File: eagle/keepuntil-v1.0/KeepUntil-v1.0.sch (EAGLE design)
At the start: 12 parts, among them Q1 CSTCR6M00G53Z, U1 ATMEGA328P-AU

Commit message: schematic work
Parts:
- added C4, C5, C6, C7: (no value), resistor:C-EUC0805
- added IC1: REG1117, burr-brown:REG1117
- added ISP, KEYPAD: (no value), pinhead:PINHD-2X3
- added LED1: (no value), led:LEDSMT1206
- added LOCK-CTRL: (no value), pinhead:PINHD-2X4
- added R7: (no value), resistor:R-EU_R0805
- added SERIAL: (no value), pinhead:PINHD-1X3
- added T1: BC846, transistor:BC846
- added X1: MINI-USB-32005-201, con-cypressindustries:MINI-USB-32005-201
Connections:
- removed net N$3: R1.1, S1.1, U1.PC6
- new net 3.3V: C2.2, C4.2, C5.2, C7.2, IC1.GND, ISP.6, LED1.C, S1.2, SERIAL.3, X1.5
- new net COL1: KEYPAD.2, U1.PB0
- new net COL2: KEYPAD.4, U1.PB1
- new net COL3: KEYPAD.6, U1.PB2
- new net LEDGRN: LOCK-CTRL.7, U1.PC0
- new net LEDRED: LOCK-CTRL.8, U1.PC1
- new net MISO: ISP.5, U1.PB4
- new net MOSI: ISP.1, U1.PB3
- new net N$12: LOCK-CTRL.2
- new net N$13: LOCK-CTRL.4
- new net N$5: C4.1, IC1.VIN, X1.1
- new net N$6: C1.2, C3.1
- new net N$7: LED1.A, R7.1
- new net N$8: C5.1, U1.AREF
- new net N$9: LOCK-CTRL.5
- new net RESET: ISP.4, R1.1, S1.1, U1.PC6
- new net ROW1: KEYPAD.1, U1.PD5
- new net ROW2: KEYPAD.3, U1.PD6
- new net ROW3: KEYPAD.5, U1.PD7
- new net RX: SERIAL.1, U1.PD0
- new net SCK: ISP.3, U1.PB5
- new net SCL: U1.PC5
- new net SERVO: LOCK-CTRL.1, U1.PD3
- new net SOLENOID: U1.PD2
- new net TX: SERIAL.2, U1.PD1
- new net VCC: C2.1, C7.1, IC1.VOUT, ISP.2, LOCK-CTRL.3, R1.2, R7.2, U1.AVCC, U1.VCC, U1.VCC_2
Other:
- moved on the sheet: C1, C2, C3, Q1, R1, R2, R3, R4, R5, R6

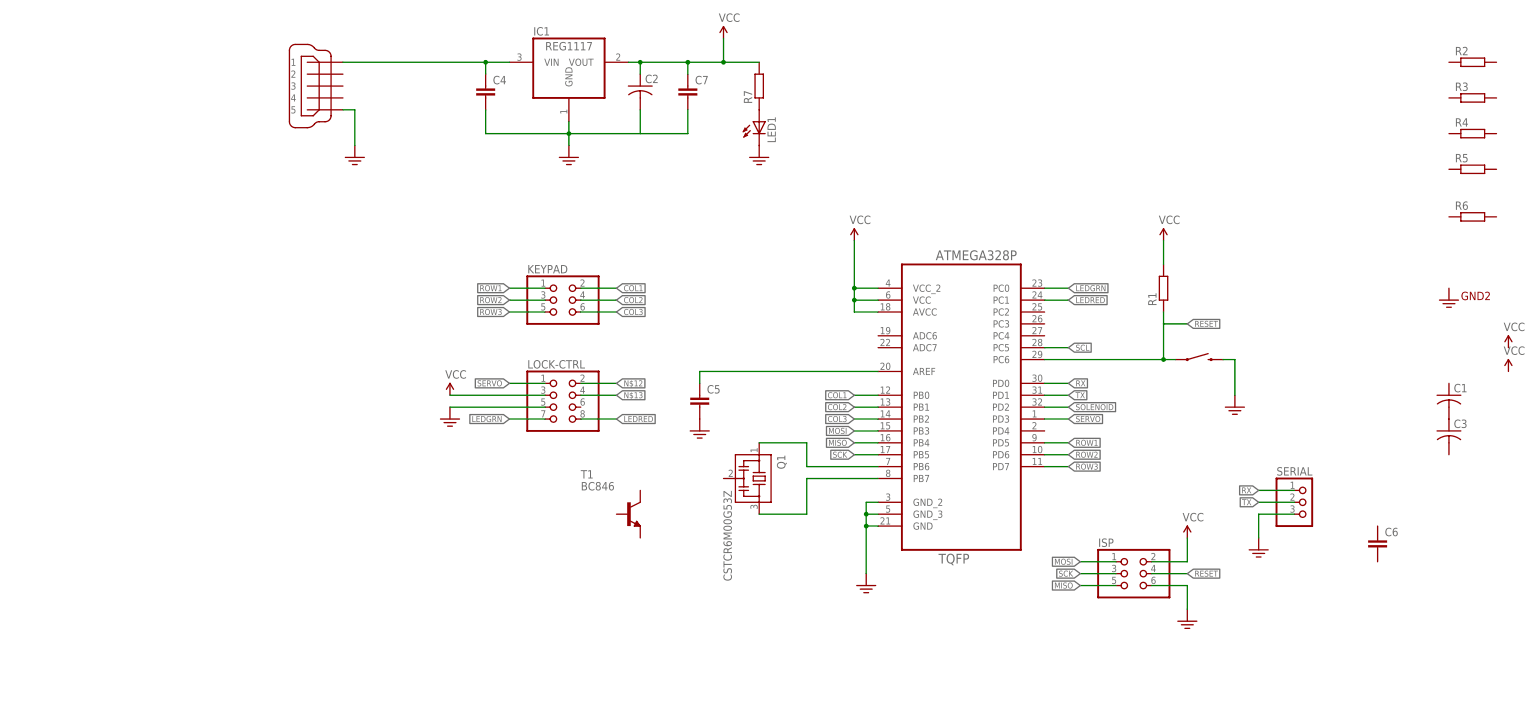
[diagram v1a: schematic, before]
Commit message: remove unnecessary eagle file
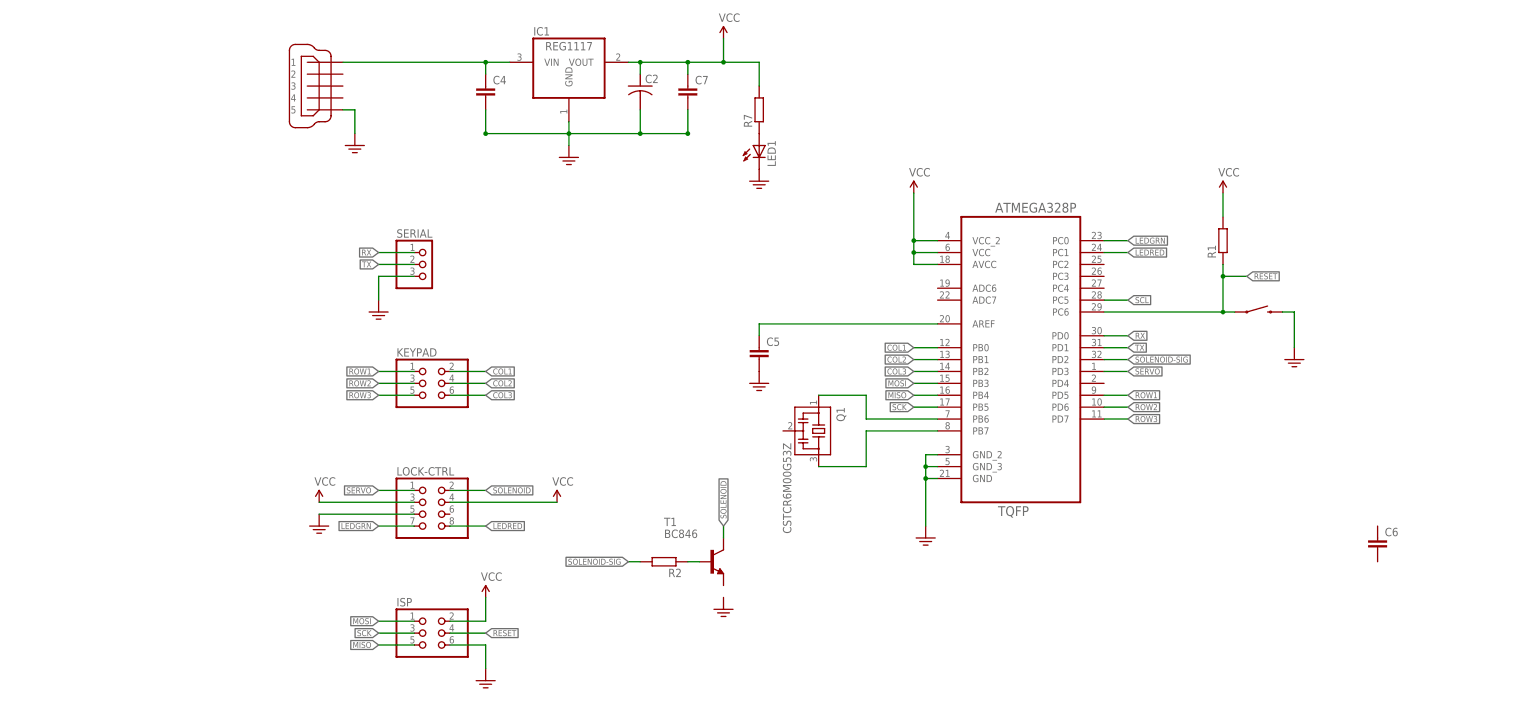
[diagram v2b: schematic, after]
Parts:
- removed C1, C3: (no value), resistor:C-USC1206
- removed R3, R4, R5, R6: (no value), resistor:R-EU_R0805
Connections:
- removed net N$12: LOCK-CTRL.2
- removed net N$13: LOCK-CTRL.4
- removed net N$6: C1.2, C3.1
- new net N$3: R2.1, T1.B
- new net SOLENOID-SIG: R2.2, U1.PD2
- net SOLENOID: now also LOCK-CTRL.2, T1.C; no longer U1.PD2
- net VCC: now also LOCK-CTRL.4
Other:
- moved on the sheet: C5, ISP, KEYPAD, LED1, LOCK-CTRL, Q1, R1, R2, R7, SERIAL, T1

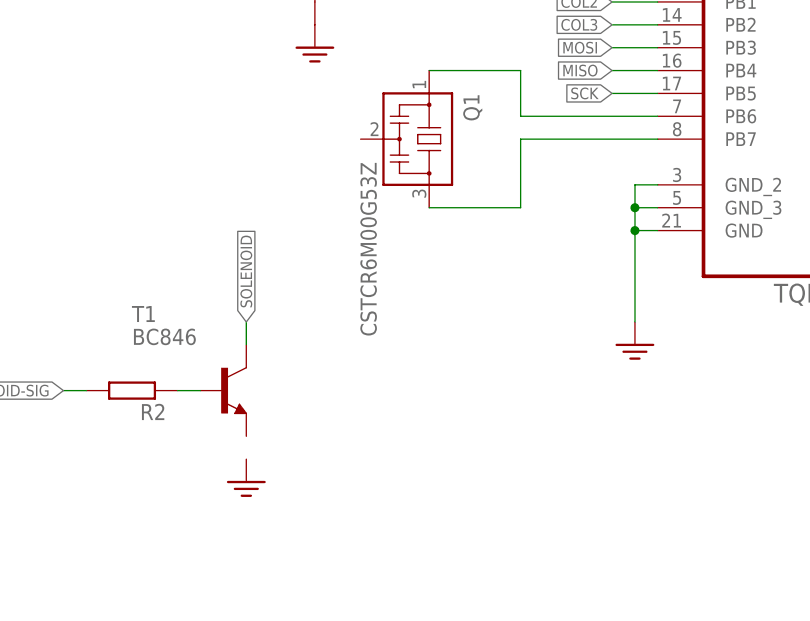
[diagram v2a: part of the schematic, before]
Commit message: update schematic
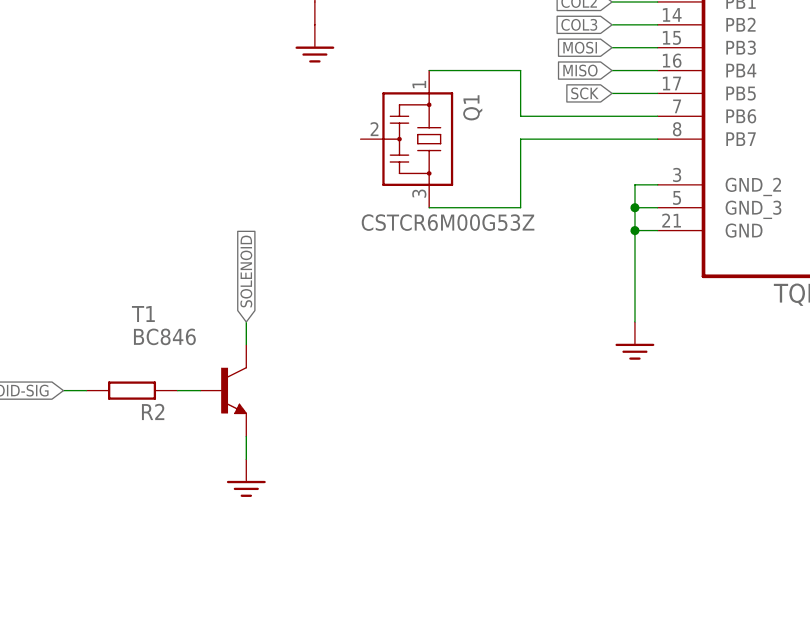
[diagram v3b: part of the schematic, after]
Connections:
- net 3.3V: now also T1.E
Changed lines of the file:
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@@
 </plain>
 <instances>
-<instance part="Q1" gate="G$1" x="137.16" y="68.58" rot="R270"/>
+<instance part="Q1" gate="G$1" x="137.16" y="68.58" smashed="yes" rot="R270">
+<attribute name="NAME" x="140.97" y="73.66" size="1.778" layer="95" rot="R270"/>
+<attribute name="VALUE" x="129.54" y="58.42" size="1.778" layer="96"/>
+</instance>
 <instance part="U1" gate="A" x="180.34" y="86.36"/>
 <instance part="S1" gate="G$1" x="231.14" y="93.98" smashed="yes"/>
@@
 <wire x1="43.18" y1="101.6" x2="43.18" y2="96.52" width="0.1524" layer="91"/>
 </segment>
+<segment>
+<pinref part="T1" gate="G$1" pin="E"/>
+<pinref part="GND2" gate="G$1" pin="3.3V"/>
+<wire x1="116.84" y1="35.56" x2="116.84" y2="33.02" width="0.1524" layer="91"/>
+</segment>
 </net>

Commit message: update schematic
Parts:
- removed C6: (no value), resistor:C-EUC0805
- added RTC: (no value), pinhead:PINHD-2X2
- IC2: MPN (none) -> LM1117 3v3
- renumbered IC1 to IC2
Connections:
- net LEDGRN renamed LED-GRN
- net LEDRED renamed LED-RED
- removed net 3.3V: C2.2, C4.2, C5.2, C7.2, IC2.GND, ISP.6, LED1.C, S1.2, SERIAL.3, T1.E, X1.5
- removed net N$4 (its old number): U1.GND, U1.GND_2, U1.GND_3
- removed net N$9: LOCK-CTRL.5
- removed net SCL: U1.PC5
- new net GND: C2.2, C4.2, C5.2, C7.2, IC2.GND, ISP.6, LED1.C, LOCK-CTRL.5, RTC.4, S1.2, SERIAL.3, T1.E, U1.GND, U1.GND_2, U1.GND_3, X1.5
- new net RTC-SCL: RTC.3, U1.PC5
- new net RTC-SDA: RTC.1, U1.PC4
- net VCC: now also RTC.2
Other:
- note added: "LM1117 5v0"
- moved on the sheet: LED1, R7

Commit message: schematic cleanup
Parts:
- removed C7: (no value), resistor:C-EUC0805
- removed SERIAL: (no value), pinhead:PINHD-1X3
- added JP1: (no value), adafruit:PINHD-1X3
- C2: value (none) -> 10uf
- C4, C5: value (none) -> 0.1uF
- R1: value (none) -> 1K
- R2: value (none) -> 10K
- R7: value (none) -> 330
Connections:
- net GND: now also JP1.3; no longer C7.2, SERIAL.3
- net RX: now also JP1.1; no longer SERIAL.1
- net TX: now also JP1.2; no longer SERIAL.2
- net VCC: no longer C7.1
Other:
- moved on the sheet: LED1, R7
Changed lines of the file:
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@@
 <part name="U1" library="Ava" deviceset="ATMEGA328P-AU" device=""/>
 <part name="S1" library="SparkFun-Electromechanical" deviceset="SWITCH-MOMENTARY-2" device="SMD-1101NE"/>
-<part name="R1" library="resistor" deviceset="R-EU_" device="R0805"/>
-<part name="C2" library="resistor" deviceset="C-US" device="C1206"/>
-<part name="C4" library="resistor" deviceset="C-EU" device="C0805"/>
-<part name="C5" library="resistor" deviceset="C-EU" device="C0805"/>
+<part name="R1" library="resistor" deviceset="R-EU_" device="R0805" value="1K"/>
+<part name="C2" library="resistor" deviceset="C-US" device="C1206" value="10uf"/>
+<part name="C4" library="resistor" deviceset="C-EU" device="C0805" value="0.1uF"/>
+<part name="C5" library="resistor" deviceset="C-EU" device="C0805" value="0.1uF"/>
 <part name="X1" library="con-cypressindustries" deviceset="MINI-USB-" device="32005-201"/>
 <part name="FRAME1" library="frames" deviceset="A4L-LOC" device=""/>
 <part name="LED1" library="led" deviceset="LED" device="SMT1206"/>
-<part name="R7" library="resistor" deviceset="R-EU_" device="R0805"/>
-<part name="C7" library="resistor" deviceset="C-EU" device="C0805"/>
+<part name="R7" library="resistor" deviceset="R-EU_" device="R0805" value="330"/>
 <part name="ISP" library="pinhead" deviceset="PINHD-2X3" device=""/>
-<part name="SERIAL" library="pinhead" deviceset="PINHD-1X3" device=""/>
 <part name="KEYPAD" library="pinhead" deviceset="PINHD-2X3" device=""/>
 <part name="LOCK-CTRL" library="pinhead" deviceset="PINHD-2X4" device=""/>
 <part name="T1" library="transistor" deviceset="BC846" device=""/>
-<part name="R2" library="resistor" deviceset="R-EU_" device="R0805"/>
+<part name="R2" library="resistor" deviceset="R-EU_" device="R0805" value="10K"/>
 <part name="RTC" library="pinhead" deviceset="PINHD-2X2" device=""/>
 <part name="P+2" library="supply1" deviceset="VCC" device=""/>
@@
 <part name="GND6" library="supply1" deviceset="GND" device=""/>
 <part name="GND7" library="supply1" deviceset="GND" device=""/>
-<part name="GND9" library="supply1" deviceset="GND" device=""/>
 <part name="GND10" library="supply1" deviceset="GND" device=""/>
 <part name="GND11" library="supply1" deviceset="GND" device=""/>
@@
 </part>
 <part name="P+1" library="supply1" deviceset="VCC" device=""/>
+<part name="JP1" library="adafruit" deviceset="PINHD-1X3" device=""/>
+<part name="GND12" library="supply1" deviceset="GND" device=""/>
 </parts>
 <sheets>
@@
 <instance part="X1" gate="G$1" x="30.48" y="142.24" smashed="yes" rot="MR0"/>
 <instance part="FRAME1" gate="G$1" x="0" y="0"/>
-<instance part="LED1" gate="G$1" x="119.38" y="132.08"/>
-<instance part="R7" gate="G$1" x="119.38" y="139.7" rot="R90"/>
-<instance part="C7" gate="G$1" x="109.22" y="142.24"/>
+<instance part="LED1" gate="G$1" x="111.76" y="132.08"/>
+<instance part="R7" gate="G$1" x="111.76" y="139.7" rot="R90"/>
 <instance part="ISP" gate="A" x="53.34" y="25.4"/>
-<instance part="SERIAL" gate="A" x="53.34" y="104.14"/>
 <instance part="KEYPAD" gate="A" x="53.34" y="78.74"/>
 <instance part="LOCK-CTRL" gate="A" x="53.34" y="50.8"/>
@@
 <instance part="P+7" gate="VCC" x="96.52" y="114.3"/>
 <instance part="GND1" gate="1" x="83.82" y="127"/>
-<instance part="GND2" gate="1" x="119.38" y="124.46"/>
+<instance part="GND2" gate="1" x="111.76" y="124.46"/>
 <instance part="GND3" gate="1" x="238.76" y="83.82"/>
 <instance part="GND4" gate="1" x="124.46" y="78.74"/>
@@
 <instance part="GND6" gate="1" x="116.84" y="30.48"/>
 <instance part="GND7" gate="1" x="66.04" y="15.24"/>
-<instance part="GND9" gate="1" x="43.18" y="93.98"/>
 <instance part="GND10" gate="1" x="96.52" y="96.52"/>
 <instance part="GND11" gate="1" x="38.1" y="129.54"/>
@@
 <instance part="P+5" gate="VCC" x="86.36" y="60.96"/>
 <instance part="IC2" gate="G$1" x="83.82" y="147.32" smashed="yes"/>
-<instance part="P+1" gate="VCC" x="129.54" y="147.32" rot="R270"/>
+<instance part="P+1" gate="VCC" x="121.92" y="147.32" rot="R270"/>
+<instance part="JP1" gate="A" x="53.34" y="104.14"/>
+<instance part="GND12" gate="1" x="43.18" y="93.98"/>
 </instances>
 <busses>
@@
 </segment>
 <segment>
-<pinref part="SERIAL" gate="A" pin="2"/>
+<pinref part="JP1" gate="A" pin="2"/>
 <wire x1="50.8" y1="104.14" x2="43.18" y2="104.14" width="0.1524" layer="91"/>
 <label x="43.18" y="104.14" size="1.27" layer="95" rot="MR0" xref="yes"/>
@@
 </segment>
 <segment>
-<pinref part="SERIAL" gate="A" pin="1"/>
-<wire x1="50.8" y1="106.68" x2="43.18" y2="106.68" width="0.1524" layer="91"/>
+<pinref part="JP1" gate="A" pin="1"/>
+<wire x1="43.18" y1="106.68" x2="50.8" y2="106.68" width="0.1524" layer="91"/>
 <label x="43.18" y="106.68" size="1.27" layer="95" rot="MR0" xref="yes"/>
 </segment>
@@
 <wire x1="96.52" y1="147.32" x2="99.06" y2="147.32" width="0.1524" layer="91"/>
 <pinref part="C2" gate="G$1" pin="1"/>
-<wire x1="99.06" y1="147.32" x2="109.22" y2="147.32" width="0.1524" layer="91"/>
-<wire x1="109.22" y1="147.32" x2="119.38" y2="147.32" width="0.1524" layer="91"/>
-<wire x1="119.38" y1="147.32" x2="127" y2="147.32" width="0.1524" layer="91"/>
+<wire x1="99.06" y1="147.32" x2="111.76" y2="147.32" width="0.1524" layer="91"/>
+<wire x1="111.76" y1="147.32" x2="119.38" y2="147.32" width="0.1524" layer="91"/>
 <wire x1="99.06" y1="147.32" x2="99.06" y2="144.78" width="0.1524" layer="91"/>
-<pinref part="C7" gate="G$1" pin="1"/>
-<wire x1="109.22" y1="147.32" x2="109.22" y2="144.78" width="0.1524" layer="91"/>
 <pinref part="R7" gate="G$1" pin="2"/>
-<wire x1="119.38" y1="147.32" x2="119.38" y2="144.78" width="0.1524" layer="91"/>
+<wire x1="111.76" y1="147.32" x2="111.76" y2="144.78" width="0.1524" layer="91"/>
 <junction x="99.06" y="147.32"/>
-<junction x="109.22" y="147.32"/>
-<junction x="119.38" y="147.32"/>
+<junction x="111.76" y="147.32"/>
 </segment>
 </net>
@@
 <wire x1="99.06" y1="132.08" x2="99.06" y2="137.16" width="0.1524" layer="91"/>
 <junction x="83.82" y="132.08"/>
-<wire x1="99.06" y1="132.08" x2="109.22" y2="132.08" width="0.1524" layer="91"/>
-<pinref part="C7" gate="G$1" pin="2"/>
-<wire x1="109.22" y1="132.08" x2="109.22" y2="137.16" width="0.1524" layer="91"/>
-<junction x="99.06" y="132.08"/>
-<junction x="109.22" y="132.08"/>
 <pinref part="GND1" gate="1" pin="GND"/>
 <pinref part="IC2" gate="G$1" pin="GND"/>
@@
 </segment>
 <segment>
-<pinref part="SERIAL" gate="A" pin="3"/>
-<wire x1="50.8" y1="101.6" x2="43.18" y2="101.6" width="0.1524" layer="91"/>
-<wire x1="43.18" y1="101.6" x2="43.18" y2="96.52" width="0.1524" layer="91"/>
-<pinref part="GND9" gate="1" pin="GND"/>
-</segment>
-<segment>
 <pinref part="RTC" gate="A" pin="4"/>
 <wire x1="88.9" y1="104.14" x2="96.52" y2="104.14" width="0.1524" layer="91"/>
@@
 <pinref part="GND8" gate="1" pin="GND"/>
 </segment>
-</net>
+<segment>
+<pinref part="JP1" gate="A" pin="3"/>
+<wire x1="50.8" y1="101.6" x2="43.18" y2="101.6" width="0.1524" layer="91"/>
+<wire x1="43.18" y1="101.6" x2="43.18" y2="96.52" width="0.1524" layer="91"/>
+<pinref part="GND12" gate="1" pin="GND"/>
+</segment>
+</net>

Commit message: board layout
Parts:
- removed S1: SWITCH-MOMENTARY-2SMD-1101NE, SparkFun-Electromechanical:SWITCH-MOMENTARY-2SMD-1101NE
- renumbered JP1 to SERIAL
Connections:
- net GND: no longer S1.2
- net RESET: no longer S1.1
- net SERVO: now also U1.ADC6; no longer U1.PD3
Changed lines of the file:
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@@
 <part name="Q1" library="murata-filter" deviceset="CSTCR" device="" technology="6M00G53Z"/>
 <part name="U1" library="Ava" deviceset="ATMEGA328P-AU" device=""/>
-<part name="S1" library="SparkFun-Electromechanical" deviceset="SWITCH-MOMENTARY-2" device="SMD-1101NE"/>
 <part name="R1" library="resistor" deviceset="R-EU_" device="R0805" value="1K"/>
 <part name="C2" library="resistor" deviceset="C-US" device="C1206" value="10uf"/>
@@
 <part name="GND1" library="supply1" deviceset="GND" device=""/>
 <part name="GND2" library="supply1" deviceset="GND" device=""/>
-<part name="GND3" library="supply1" deviceset="GND" device=""/>
 <part name="GND4" library="supply1" deviceset="GND" device=""/>
 <part name="GND5" library="supply1" deviceset="GND" device=""/>
@@
 </part>
 <part name="P+1" library="supply1" deviceset="VCC" device=""/>
-<part name="JP1" library="adafruit" deviceset="PINHD-1X3" device=""/>
+<part name="SERIAL" library="adafruit" deviceset="PINHD-1X3" device=""/>
 <part name="GND12" library="supply1" deviceset="GND" device=""/>
 </parts>
@@
 </instance>
 <instance part="U1" gate="A" x="180.34" y="86.36"/>
-<instance part="S1" gate="G$1" x="231.14" y="93.98" smashed="yes"/>
 <instance part="R1" gate="G$1" x="223.52" y="109.22" rot="R90"/>
 <instance part="C2" gate="G$1" x="99.06" y="142.24"/>
@@
 <instance part="GND1" gate="1" x="83.82" y="127"/>
 <instance part="GND2" gate="1" x="111.76" y="124.46"/>
-<instance part="GND3" gate="1" x="238.76" y="83.82"/>
 <instance part="GND4" gate="1" x="124.46" y="78.74"/>
 <instance part="GND5" gate="1" x="160.02" y="45.72"/>
@@
 <instance part="IC2" gate="G$1" x="83.82" y="147.32" smashed="yes"/>
 <instance part="P+1" gate="VCC" x="121.92" y="147.32" rot="R270"/>
-<instance part="JP1" gate="A" x="53.34" y="104.14"/>
+<instance part="SERIAL" gate="A" x="53.34" y="104.14"/>
 <instance part="GND12" gate="1" x="43.18" y="93.98"/>
 </instances>
@@
 <segment>
 <pinref part="U1" gate="A" pin="PC6"/>
-<pinref part="S1" gate="G$1" pin="1"/>
 <wire x1="198.12" y1="93.98" x2="223.52" y2="93.98" width="0.1524" layer="91"/>
 <pinref part="R1" gate="G$1" pin="1"/>
-<wire x1="223.52" y1="93.98" x2="226.06" y2="93.98" width="0.1524" layer="91"/>
 <wire x1="223.52" y1="104.14" x2="223.52" y2="101.6" width="0.1524" layer="91"/>
-<junction x="223.52" y="93.98"/>
 <wire x1="223.52" y1="101.6" x2="223.52" y2="93.98" width="0.1524" layer="91"/>
 <wire x1="223.52" y1="101.6" x2="228.6" y2="101.6" width="0.1524" layer="91"/>
@@
 </segment>
 <segment>
-<pinref part="JP1" gate="A" pin="2"/>
+<pinref part="SERIAL" gate="A" pin="2"/>
 <wire x1="50.8" y1="104.14" x2="43.18" y2="104.14" width="0.1524" layer="91"/>
 <label x="43.18" y="104.14" size="1.27" layer="95" rot="MR0" xref="yes"/>
@@
 </segment>
 <segment>
-<pinref part="JP1" gate="A" pin="1"/>
+<pinref part="SERIAL" gate="A" pin="1"/>
 <wire x1="43.18" y1="106.68" x2="50.8" y2="106.68" width="0.1524" layer="91"/>
 <label x="43.18" y="106.68" size="1.27" layer="95" rot="MR0" xref="yes"/>
@@
 <net name="SERVO" class="0">
 <segment>
-<pinref part="U1" gate="A" pin="PD3"/>
-<wire x1="198.12" y1="81.28" x2="203.2" y2="81.28" width="0.1524" layer="91"/>
-<label x="203.2" y="81.28" size="1.27" layer="95" xref="yes"/>
-</segment>
-<segment>
 <pinref part="LOCK-CTRL" gate="A" pin="1"/>
 <wire x1="50.8" y1="55.88" x2="43.18" y2="55.88" width="0.1524" layer="91"/>
 <label x="43.18" y="55.88" size="1.27" layer="95" rot="MR0" xref="yes"/>
+</segment>
+<segment>
+<pinref part="U1" gate="A" pin="ADC6"/>
+<wire x1="162.56" y1="99.06" x2="157.48" y2="99.06" width="0.1524" layer="91"/>
+<label x="157.48" y="99.06" size="1.27" layer="95" rot="MR0" xref="yes"/>
 </segment>
 </net>
@@
 </segment>
 <segment>
-<pinref part="S1" gate="G$1" pin="2"/>
-<wire x1="236.22" y1="93.98" x2="238.76" y2="93.98" width="0.1524" layer="91"/>
-<wire x1="238.76" y1="93.98" x2="238.76" y2="86.36" width="0.1524" layer="91"/>
-<pinref part="GND3" gate="1" pin="GND"/>
-</segment>
-<segment>
 <pinref part="C5" gate="G$1" pin="2"/>
 <pinref part="GND4" gate="1" pin="GND"/>
@@
 </segment>
 <segment>
-<pinref part="JP1" gate="A" pin="3"/>
+<pinref part="SERIAL" gate="A" pin="3"/>
 <wire x1="50.8" y1="101.6" x2="43.18" y2="101.6" width="0.1524" layer="91"/>
 <wire x1="43.18" y1="101.6" x2="43.18" y2="96.52" width="0.1524" layer="91"/>
